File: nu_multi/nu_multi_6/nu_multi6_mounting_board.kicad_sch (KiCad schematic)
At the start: 13 parts, among them J1 CONN_01X02, J10 CONN_01X03, J11 CONN_01X02, J12 CONN_01X03, J13 CONN_01X14, J2 CONN_01X03, J3 CONN_01X02, J4 CONN_01X03, J5 CONN_01X02, J6 CONN_01X03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

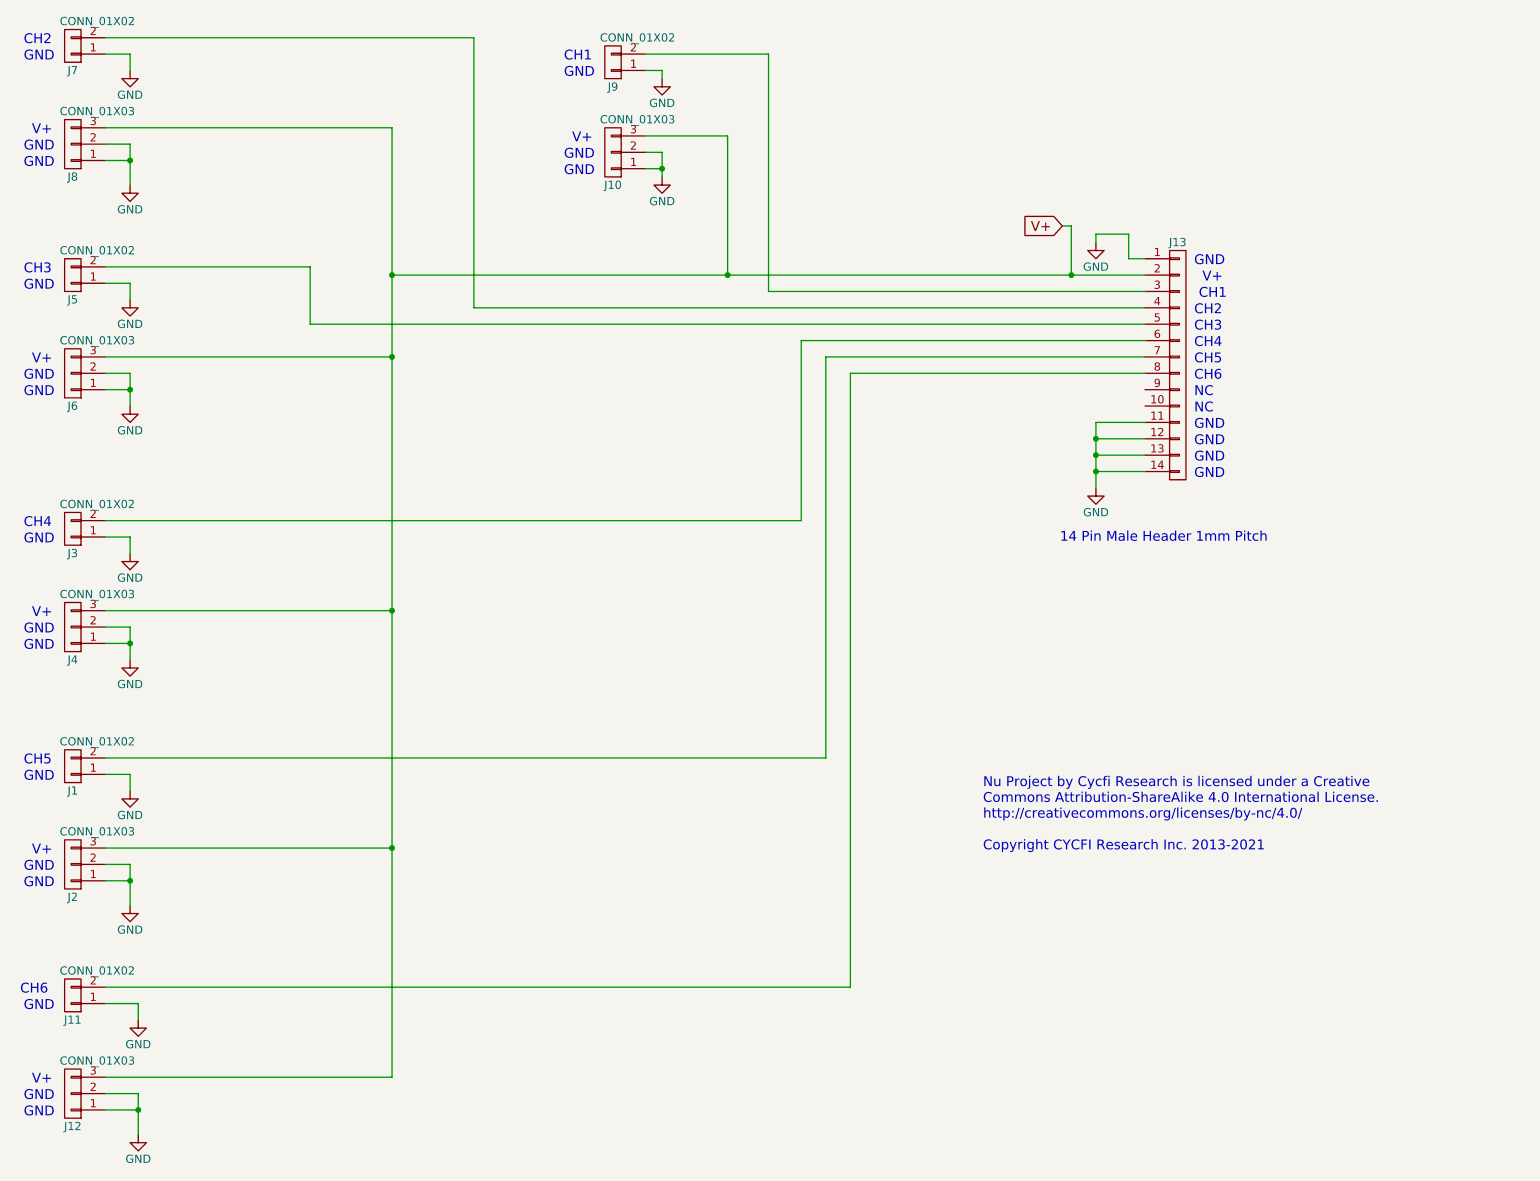
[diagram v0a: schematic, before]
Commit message: Upgraded schematics and PCB layout using Nu Capsule footprint
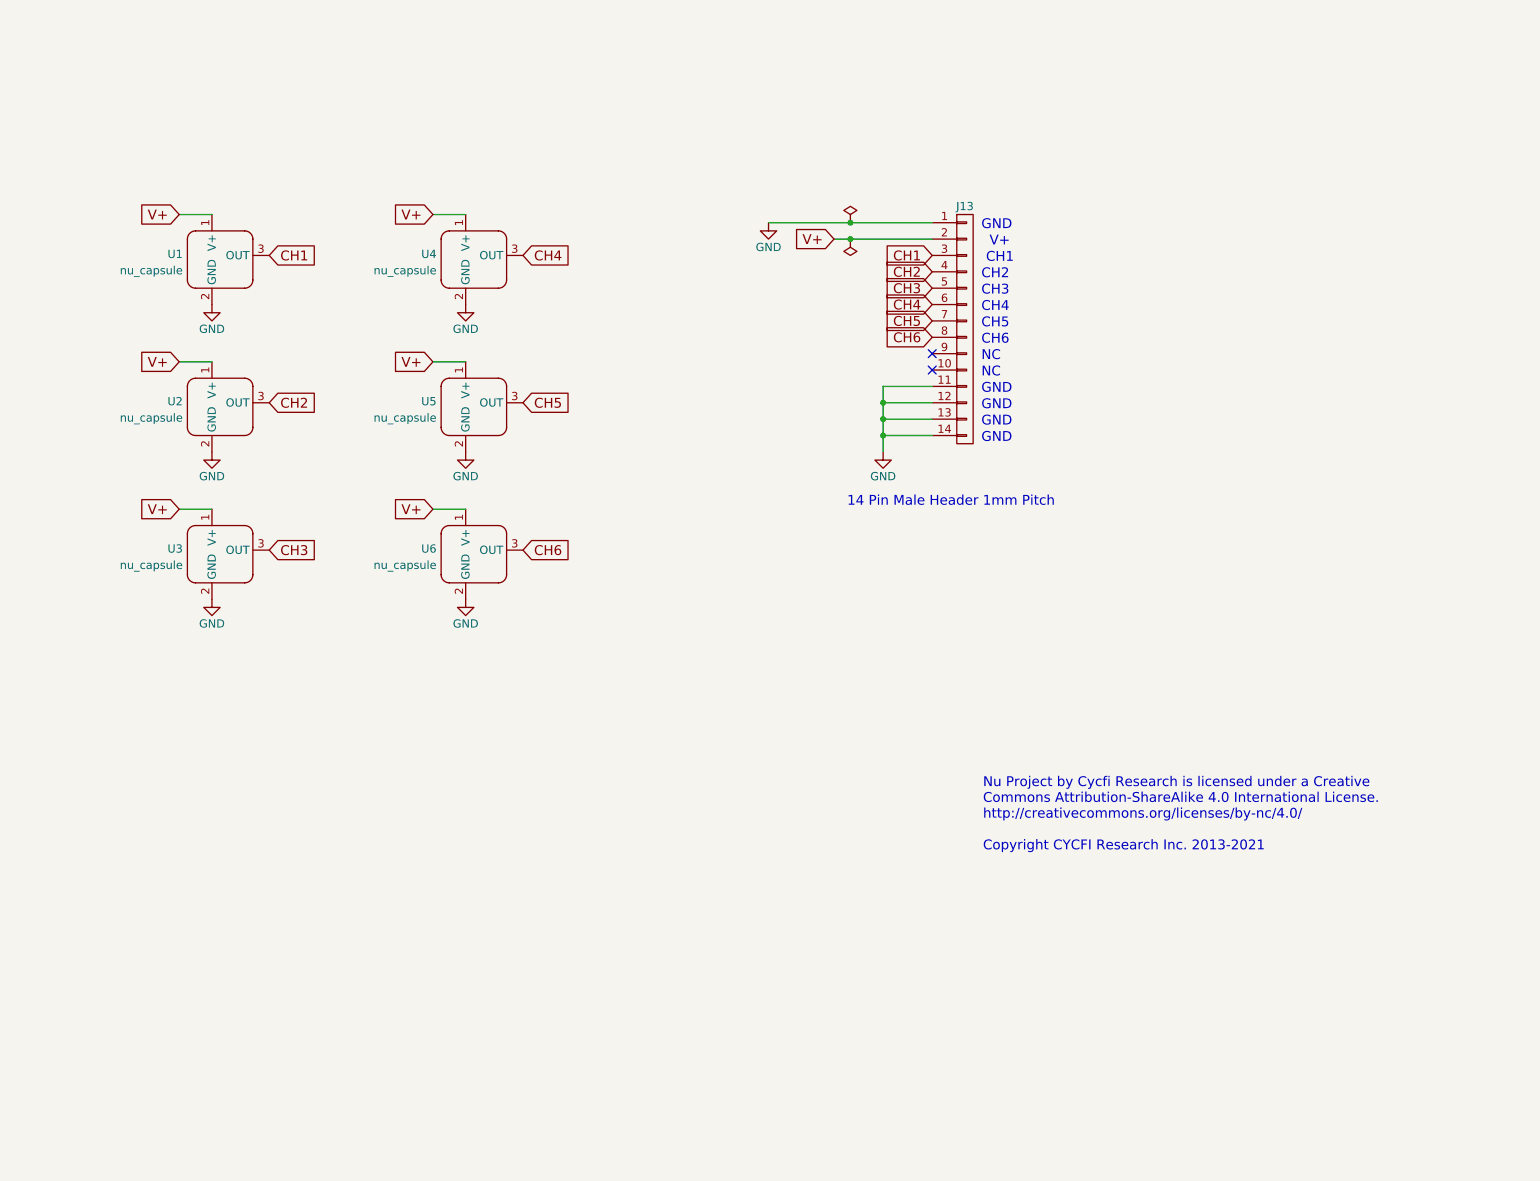
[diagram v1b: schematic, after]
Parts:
- removed J1, J11, J3, J5, J7, J9: CONN_01X02, Pin_Headers:Pin_Header_Straight_1x02_Pitch2.00mm, symbol cycfi_library:CONN_01X02
- removed J10, J12, J2, J4, J6, J8: CONN_01X03, Pin_Headers:Pin_Header_Straight_1x03_Pitch2.00mm, symbol cycfi_library:CONN_01X03
- added U1, U2, U3, U4, U5, U6: nu_capsule, cycfi_library:nu_capsule, symbol cycfi_library:nu_capsule
- J13: symbol cycfi_library:CONN_01X14 -> cycfi_library:conn_1x14
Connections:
- net GND: now also U1.2 (GND), U2.2 (GND), U3.2 (GND), U4.2 (GND), U5.2 (GND), U6.2 (GND)
- net V+: now also U1.1 (V+), U2.1 (V+), U3.1 (V+), U4.1 (V+), U5.1 (V+), U6.1 (V+)
- net CH5: now reaches J13.7 (P7)
- net CH5: now also U5.3 (OUT)
- net CH4: now reaches J13.6 (P6)
- net CH4: now also U4.3 (OUT)
- net CH3: now reaches J13.5 (P5)
- net CH3: now also U3.3 (OUT)
- net CH2: now reaches J13.4 (P4)
- net CH2: now also U2.3 (OUT)
- net CH6: now reaches J13.8 (P8)
- net CH6: now also U6.3 (OUT)
- net CH1: now reaches J13.3 (P3)
- net CH1: now also U1.3 (OUT)
- no-connect marks 0 -> 2
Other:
- moved on the sheet: J13
